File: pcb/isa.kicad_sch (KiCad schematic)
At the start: 9 parts, among them J1 Bus_ISA_16bit, J10 ISA_DEBUG, J2 Bus_ISA_16bit

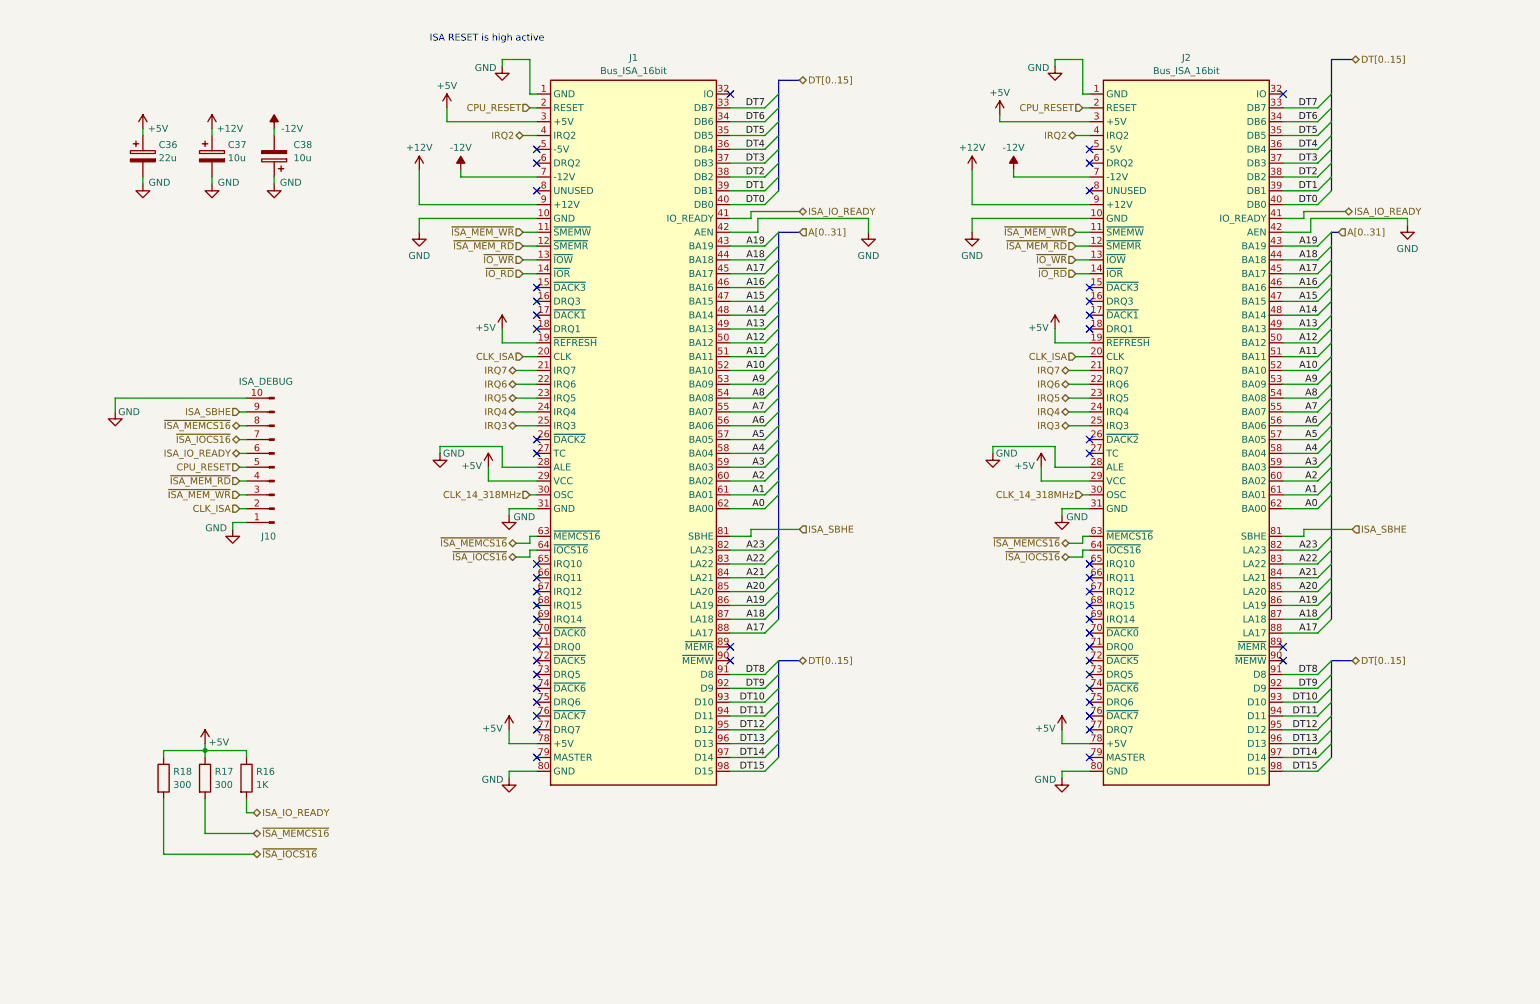
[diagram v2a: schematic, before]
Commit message: isa diagram aligned, removed ISA_DEBUG connector, updated ISA symbols, added ISA_BALE jumper
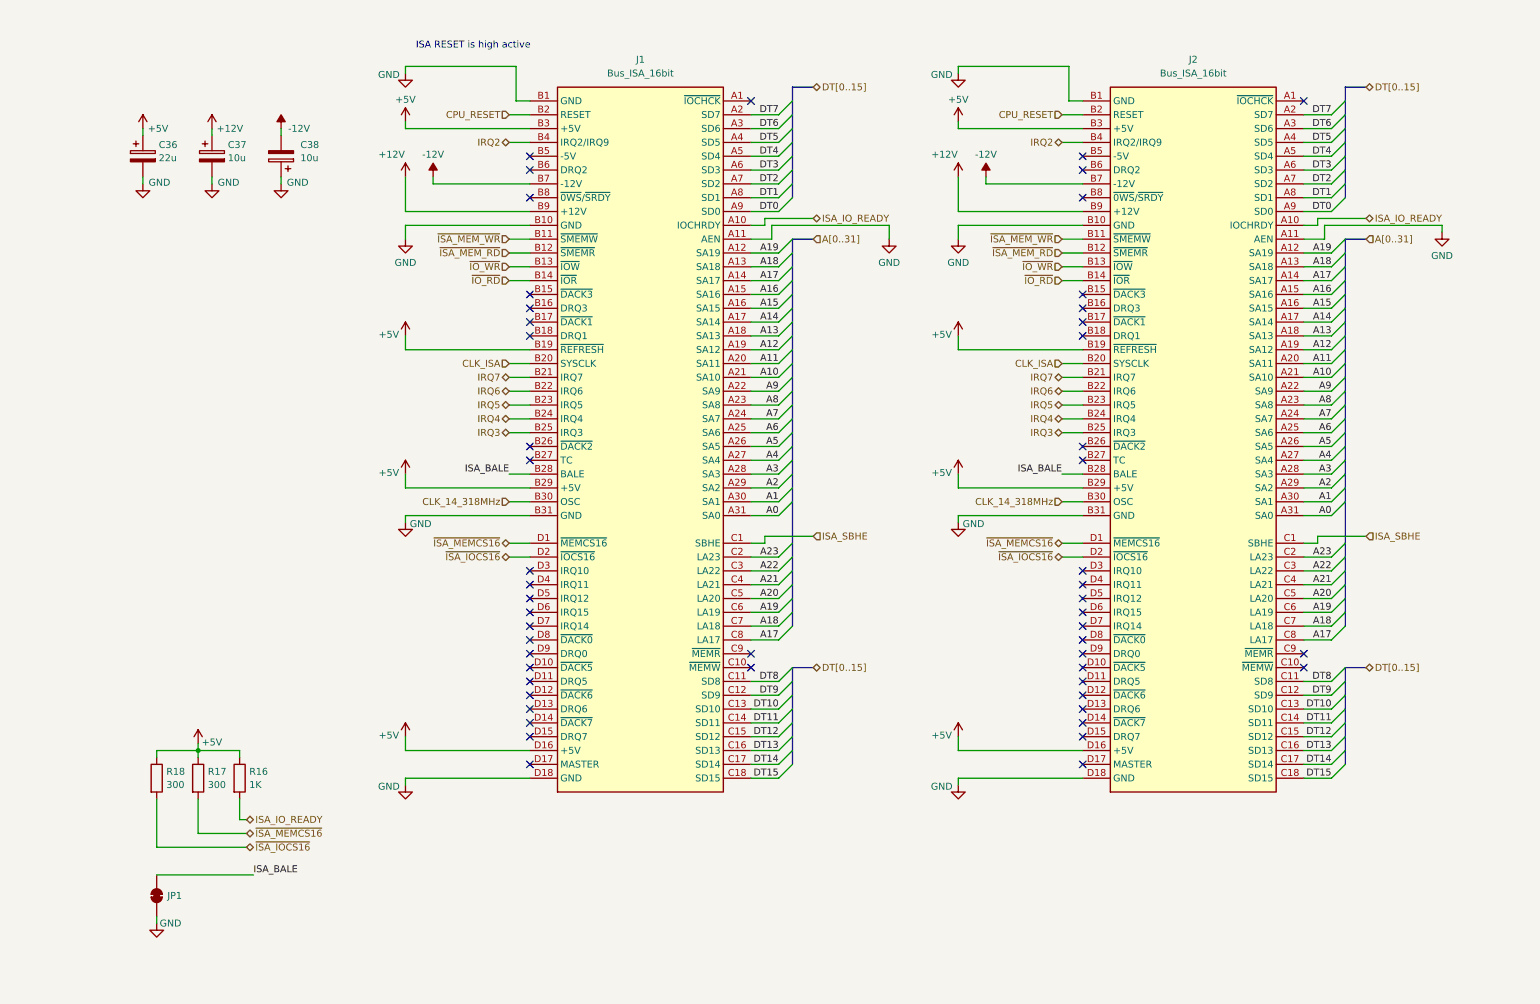
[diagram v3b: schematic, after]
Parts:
- removed J10: ISA_DEBUG, Connector_PinHeader_2.54mm:PinHeader_1x10_P2.54mm_Vertical, symbol Connector:Conn_01x10_Pin
- added JP1: SolderJumper_2_Bridged, Jumper:SolderJumper-2_P1.3mm_Bridged_RoundedPad1.0x1.5mm, symbol Jumper:SolderJumper_2_Bridged
- J1, J2: footprint ultimateretro:ISA16 -> 486custom:ISA16; symbol Connector:Bus_ISA_16bit -> sbc486_additional:Bus_ISA_16bit_Slot
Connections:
- net +12V: now also J1.B9 (+12V), J2.B9 (+12V); no longer J1.9 (+12V), J2.9 (+12V)
- net +5V: now also J1.B19 (~{REFRESH}), J1.B29 (+5V), J1.B3 (+5V), J1.D16 (+5V), J2.B19 (~{REFRESH}), J2.B29 (+5V), J2.B3 (+5V), J2.D16 (+5V); no longer J1.19 (~{REFRESH}), J1.29 (VCC), J1.3 (+5V), J1.78 (+5V), J2.19 (~{REFRESH}), J2.29 (VCC), J2.3 (+5V), J2.78 (+5V)
- net -12V: now also J1.B7 (-12V), J2.B7 (-12V); no longer J1.7 (-12V), J2.7 (-12V)
- net A0: now also J1.A31 (SA0), J2.A31 (SA0); no longer J1.62 (BA00), J2.62 (BA00)
- net A1: now also J1.A30 (SA1), J2.A30 (SA1); no longer J1.61 (BA01), J2.61 (BA01)
- net A10: now also J1.A21 (SA10), J2.A21 (SA10); no longer J1.52 (BA10), J2.52 (BA10)
- net A11: now also J1.A20 (SA11), J2.A20 (SA11); no longer J1.51 (BA11), J2.51 (BA11)
- net A12: now also J1.A19 (SA12), J2.A19 (SA12); no longer J1.50 (BA12), J2.50 (BA12)
- net A13: now also J1.A18 (SA13), J2.A18 (SA13); no longer J1.49 (BA13), J2.49 (BA13)
- net A14: now also J1.A17 (SA14), J2.A17 (SA14); no longer J1.48 (BA14), J2.48 (BA14)
- net A15: now also J1.A16 (SA15), J2.A16 (SA15); no longer J1.47 (BA15), J2.47 (BA15)
- net A16: now also J1.A15 (SA16), J2.A15 (SA16); no longer J1.46 (BA16), J2.46 (BA16)
- net A17: now also J1.A14 (SA17), J1.C8 (LA17), J2.A14 (SA17), J2.C8 (LA17); no longer J1.45 (BA17), J1.88 (LA17), J2.45 (BA17), J2.88 (LA17)
- net A18: now also J1.A13 (SA18), J1.C7 (LA18), J2.A13 (SA18), J2.C7 (LA18); no longer J1.44 (BA18), J1.87 (LA18), J2.44 (BA18), J2.87 (LA18)
- net A19: now also J1.A12 (SA19), J1.C6 (LA19), J2.A12 (SA19), J2.C6 (LA19); no longer J1.43 (BA19), J1.86 (LA19), J2.43 (BA19), J2.86 (LA19)
- net A2: now also J1.A29 (SA2), J2.A29 (SA2); no longer J1.60 (BA02), J2.60 (BA02)
- net A20: now also J1.C5 (LA20), J2.C5 (LA20); no longer J1.85 (LA20), J2.85 (LA20)
- net A21: now also J1.C4 (LA21), J2.C4 (LA21); no longer J1.84 (LA21), J2.84 (LA21)
- net A22: now also J1.C3 (LA22), J2.C3 (LA22); no longer J1.83 (LA22), J2.83 (LA22)
- net A23: now also J1.C2 (LA23), J2.C2 (LA23); no longer J1.82 (LA23), J2.82 (LA23)
- net A3: now also J1.A28 (SA3), J2.A28 (SA3); no longer J1.59 (BA03), J2.59 (BA03)
- net A4: now also J1.A27 (SA4), J2.A27 (SA4); no longer J1.58 (BA04), J2.58 (BA04)
- net A5: now also J1.A26 (SA5), J2.A26 (SA5); no longer J1.57 (BA05), J2.57 (BA05)
- net A6: now also J1.A25 (SA6), J2.A25 (SA6); no longer J1.56 (BA06), J2.56 (BA06)
- net A7: now also J1.A24 (SA7), J2.A24 (SA7); no longer J1.55 (BA07), J2.55 (BA07)
- net A8: now also J1.A23 (SA8), J2.A23 (SA8); no longer J1.54 (BA08), J2.54 (BA08)
- net A9: now also J1.A22 (SA9), J2.A22 (SA9); no longer J1.53 (BA09), J2.53 (BA09)
- net CLK_14_318MHz: now also J1.B30 (OSC), J2.B30 (OSC); no longer J1.30 (OSC), J2.30 (OSC)
- net CLK_ISA: now also J1.B20 (SYSCLK), J2.B20 (SYSCLK); no longer J1.20 (CLK), J2.20 (CLK)
- net CPU_RESET: now also J1.B2 (RESET), J2.B2 (RESET); no longer J1.2 (RESET), J2.2 (RESET)
- net DT0: now also J1.A9 (SD0), J2.A9 (SD0); no longer J1.40 (DB0), J2.40 (DB0)
- net DT1: now also J1.A8 (SD1), J2.A8 (SD1); no longer J1.39 (DB1), J2.39 (DB1)
- net DT10: now also J1.C13 (SD10), J2.C13 (SD10); no longer J1.93 (D10), J2.93 (D10)
- net DT11: now also J1.C14 (SD11), J2.C14 (SD11); no longer J1.94 (D11), J2.94 (D11)
- net DT12: now also J1.C15 (SD12), J2.C15 (SD12); no longer J1.95 (D12), J2.95 (D12)
- net DT13: now also J1.C16 (SD13), J2.C16 (SD13); no longer J1.96 (D13), J2.96 (D13)
- net DT14: now also J1.C17 (SD14), J2.C17 (SD14); no longer J1.97 (D14), J2.97 (D14)
- net DT15: now also J1.C18 (SD15), J2.C18 (SD15); no longer J1.98 (D15), J2.98 (D15)
- net DT2: now also J1.A7 (SD2), J2.A7 (SD2); no longer J1.38 (DB2), J2.38 (DB2)
- net DT3: now also J1.A6 (SD3), J2.A6 (SD3); no longer J1.37 (DB3), J2.37 (DB3)
- net DT4: now also J1.A5 (SD4), J2.A5 (SD4); no longer J1.36 (DB4), J2.36 (DB4)
- net DT5: now also J1.A4 (SD5), J2.A4 (SD5); no longer J1.35 (DB5), J2.35 (DB5)
- net DT6: now also J1.A3 (SD6), J2.A3 (SD6); no longer J1.34 (DB6), J2.34 (DB6)
- net DT7: now also J1.A2 (SD7), J2.A2 (SD7); no longer J1.33 (DB7), J2.33 (DB7)
- net DT8: now also J1.C11 (SD8), J2.C11 (SD8); no longer J1.91 (D8), J2.91 (D8)
- net DT9: now also J1.C12 (SD9), J2.C12 (SD9); no longer J1.92 (D9), J2.92 (D9)
- net GND: now also J1.A11 (AEN), J1.B1 (GND), J1.B10 (GND), J1.B31 (GND), J1.D18 (GND), J2.A11 (AEN), J2.B1 (GND), J2.B10 (GND), J2.B31 (GND), J2.D18 (GND), JP1.1 (A); no longer J1.1 (GND), J1.10 (GND), J1.28 (ALE), J1.31 (GND), J1.42 (AEN), J1.80 (GND), J2.1 (GND), J2.10 (GND), J2.28 (ALE), J2.31 (GND), J2.42 (AEN), J2.80 (GND)
- net IRQ2: now also J1.B4 (IRQ2/IRQ9), J2.B4 (IRQ2/IRQ9); no longer J1.4 (IRQ2), J2.4 (IRQ2)
- net IRQ3: now also J1.B25 (IRQ3), J2.B25 (IRQ3); no longer J1.25 (IRQ3), J2.25 (IRQ3)
- net IRQ4: now also J1.B24 (IRQ4), J2.B24 (IRQ4); no longer J1.24 (IRQ4), J2.24 (IRQ4)
- net IRQ5: now also J1.B23 (IRQ5), J2.B23 (IRQ5); no longer J1.23 (IRQ5), J2.23 (IRQ5)
- net IRQ6: now also J1.B22 (IRQ6), J2.B22 (IRQ6); no longer J1.22 (IRQ6), J2.22 (IRQ6)
- net IRQ7: now also J1.B21 (IRQ7), J2.B21 (IRQ7); no longer J1.21 (IRQ7), J2.21 (IRQ7)
- net ISA_IO_READY: now also J1.A10 (IOCHRDY), J2.A10 (IOCHRDY); no longer J1.41 (IO_READY), J2.41 (IO_READY)
- net ISA_SBHE: now also J1.C1 (SBHE), J2.C1 (SBHE); no longer J1.81 (SBHE), J2.81 (SBHE)
- net ~{IO_RD}: now also J1.B14 (~{IOR}), J2.B14 (~{IOR}); no longer J1.14 (~{IOR}), J2.14 (~{IOR})
- net ~{IO_WR}: now also J1.B13 (~{IOW}), J2.B13 (~{IOW}); no longer J1.13 (~{IOW}), J2.13 (~{IOW})
- net ~{ISA_IOCS16}: now also J1.D2 (~{IOCS16}), J2.D2 (~{IOCS16}); no longer J1.64 (~{IOCS16}), J2.64 (~{IOCS16})
- net ~{ISA_MEMCS16}: now also J1.D1 (~{MEMCS16}), J2.D1 (~{MEMCS16}); no longer J1.63 (~{MEMCS16}), J2.63 (~{MEMCS16})
- net ~{ISA_MEM_RD}: now also J1.B12 (~{SMEMR}), J2.B12 (~{SMEMR}); no longer J1.12 (~{SMEMR}), J2.12 (~{SMEMR})
- net ~{ISA_MEM_WR}: now also J1.B11 (~{SMEMW}), J2.B11 (~{SMEMW}); no longer J1.11 (~{SMEMW}), J2.11 (~{SMEMW})
- new net ISA_BALE: J1.B28 (BALE), J2.B28 (BALE), JP1.2 (B)
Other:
- moved on the sheet: C38, J1, J2, R16, R17, R18

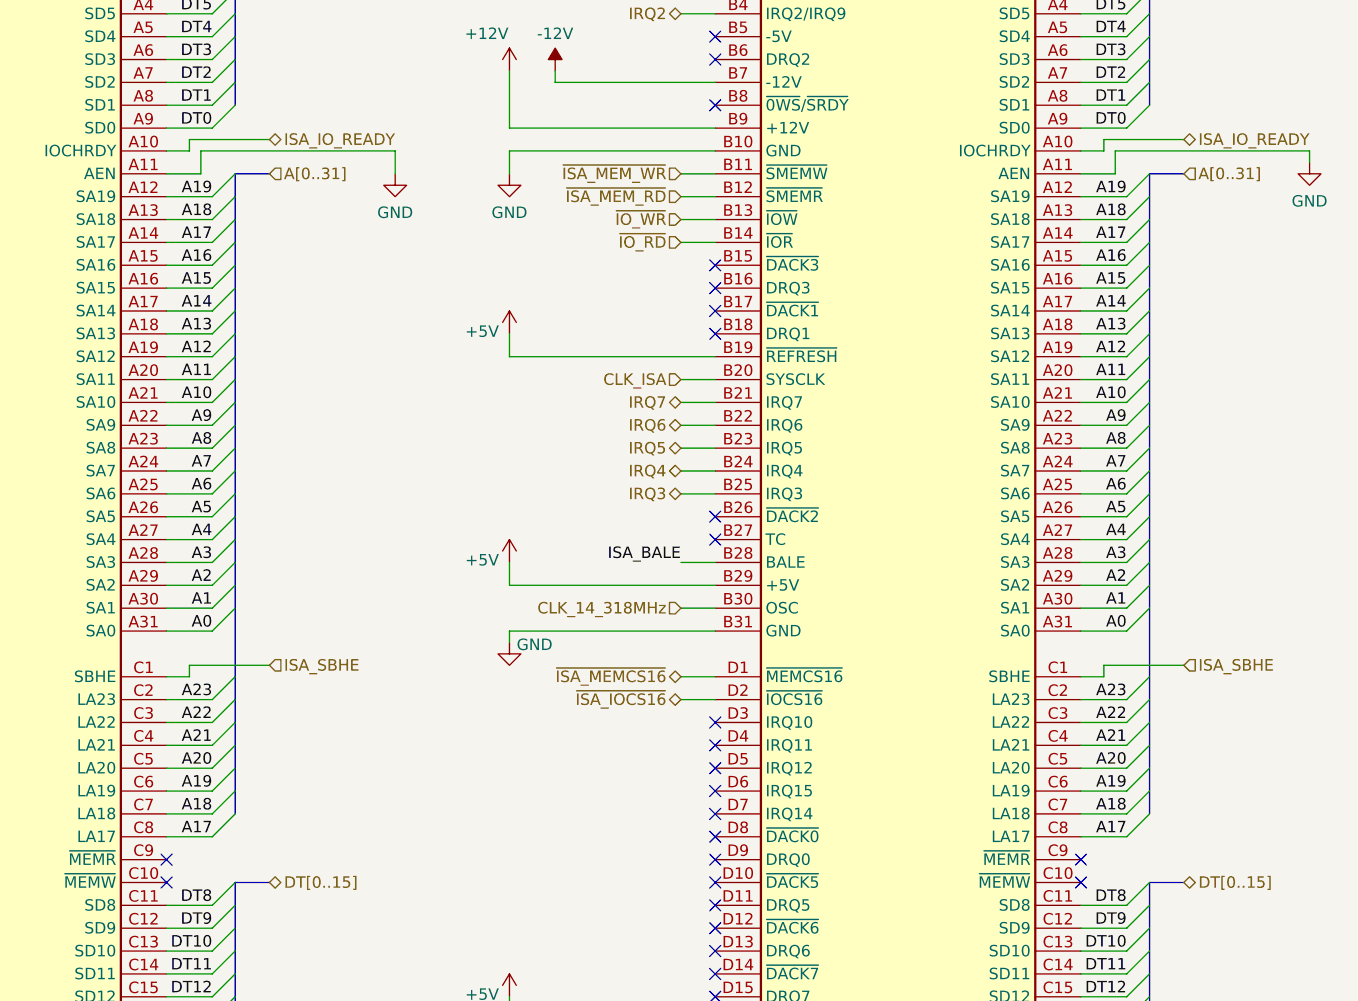
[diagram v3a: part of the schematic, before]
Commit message: moving ISA to slow SA side of CPU address bus
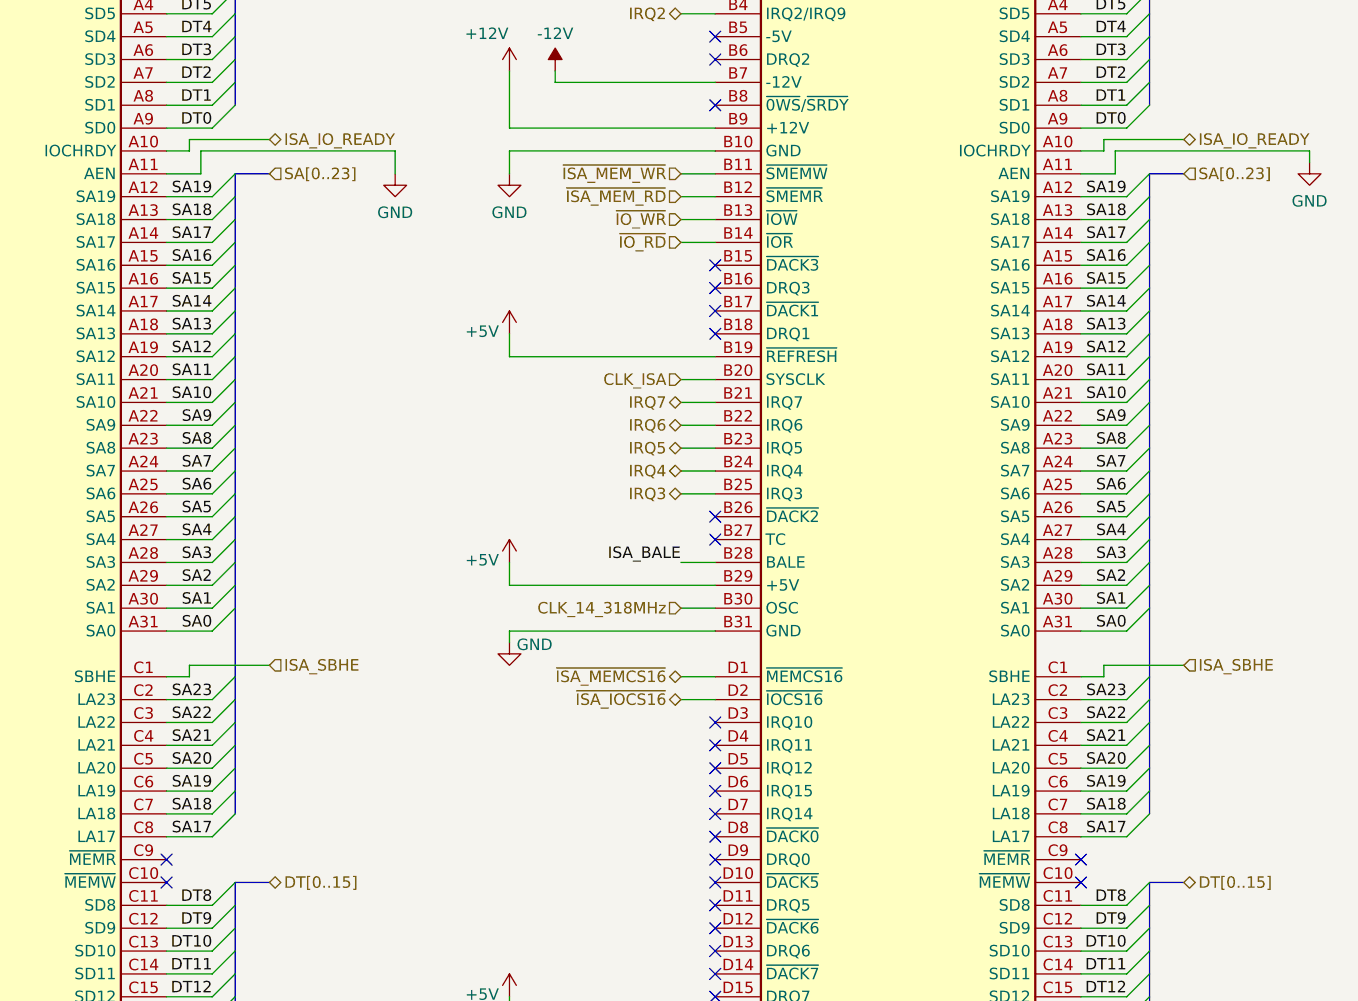
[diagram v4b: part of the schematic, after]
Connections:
- net A0 renamed SA0
- net A1 renamed SA1
- net A10 renamed SA10
- net A11 renamed SA11
- net A12 renamed SA12
- net A13 renamed SA13
- net A14 renamed SA14
- net A15 renamed SA15
- net A16 renamed SA16
- net A17 renamed SA17
- net A18 renamed SA18
- net A19 renamed SA19
- net A2 renamed SA2
- net A20 renamed SA20
- net A21 renamed SA21
- net A22 renamed SA22
- net A23 renamed SA23
- net A3 renamed SA3
- net A4 renamed SA4
- net A5 renamed SA5
- net A6 renamed SA6
- net A7 renamed SA7
- net A8 renamed SA8
- net A9 renamed SA9
